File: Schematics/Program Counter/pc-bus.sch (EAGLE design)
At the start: 22 parts

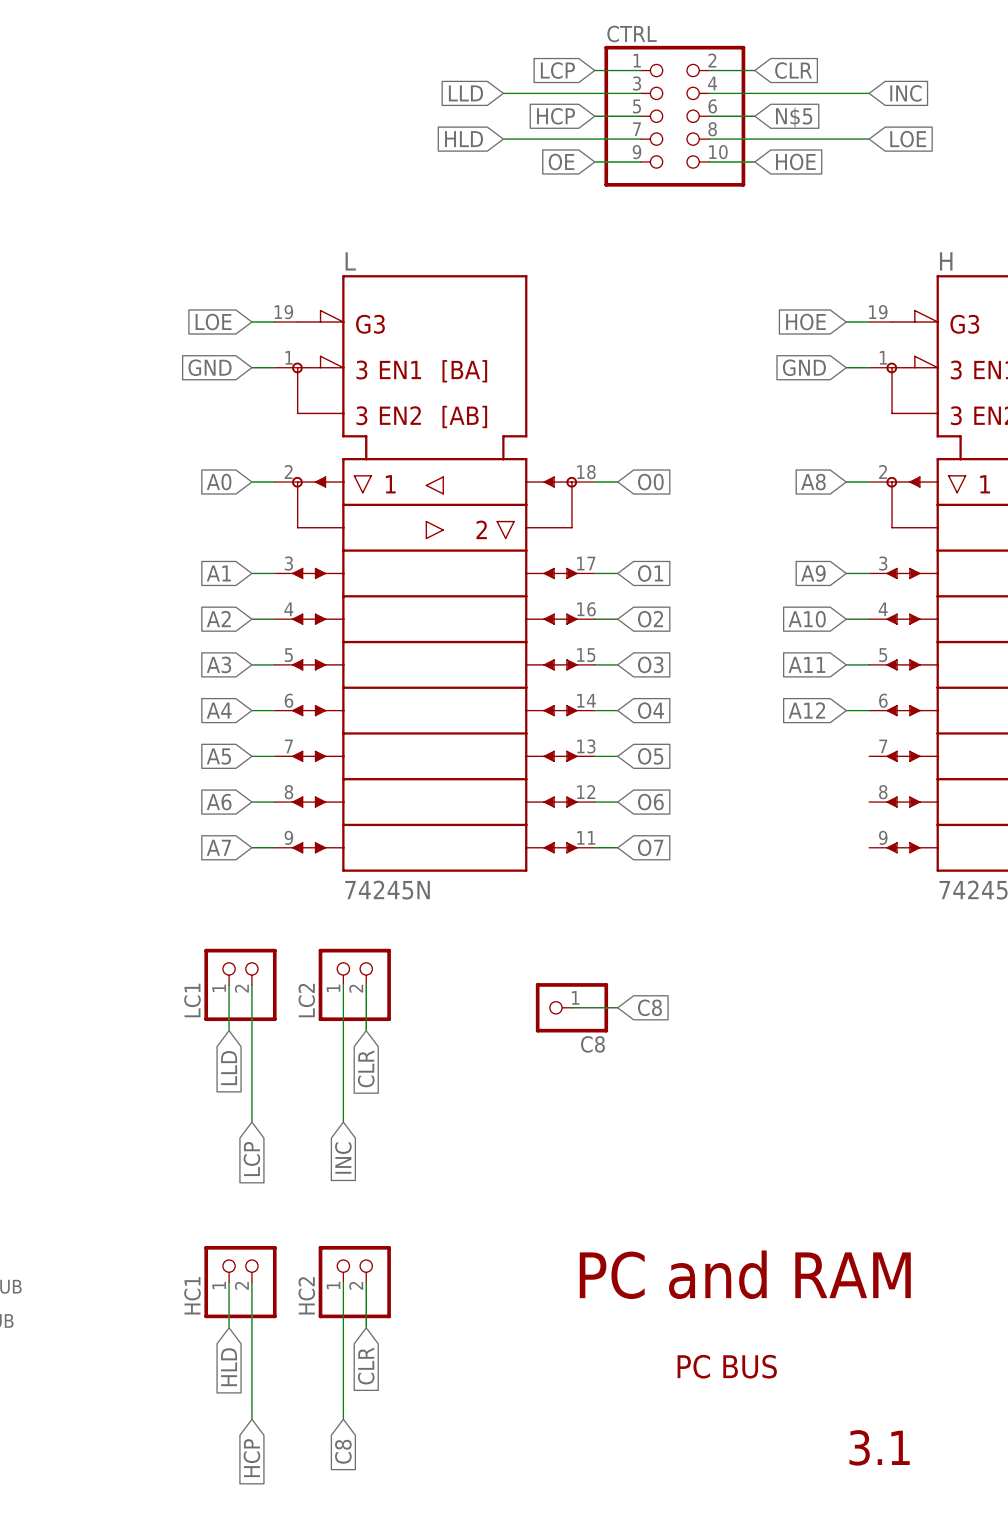
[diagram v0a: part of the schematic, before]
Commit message: Fixed DIR pin on HOE and LOE. Found when I was testing real brd.
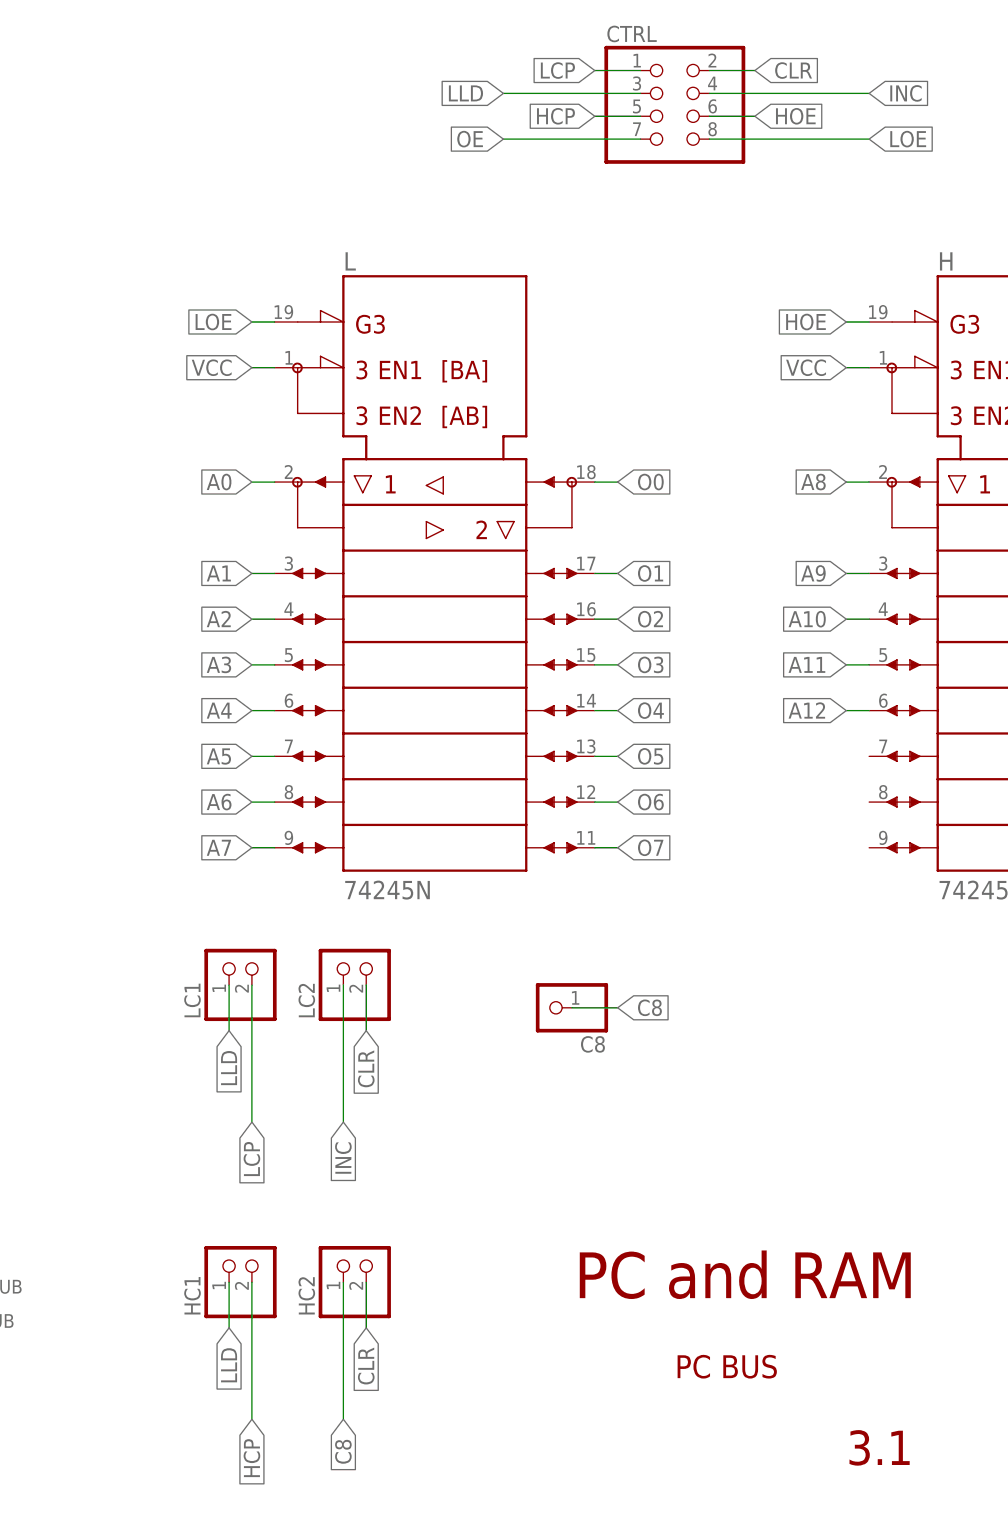
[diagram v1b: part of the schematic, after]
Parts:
- CTRL: device pinhead:PINHD-2X5 -> pinhead:PINHD-2X4
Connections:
- removed net HLD: CTRL.7, HC1.1
- removed net N$5: CTRL.6
- net GND: no longer H1.DIR, L1.DIR
- net HOE: now also CTRL.6; no longer CTRL.10
- net LLD: now also HC1.1
- net OE: now also CTRL.7; no longer CTRL.9
- net VCC: now also H1.DIR, L1.DIR
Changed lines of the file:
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@@
 <part name="H" library="74ttl-din" library_urn="urn:adsk.eagle:library:84" deviceset="74*245" device="N" package3d_urn="urn:adsk.eagle:package:16429/2"/>
 <part name="L" library="74ttl-din" library_urn="urn:adsk.eagle:library:84" deviceset="74*245" device="N" package3d_urn="urn:adsk.eagle:package:16429/2"/>
-<part name="CTRL" library="pinhead" library_urn="urn:adsk.eagle:library:325" deviceset="PINHD-2X5" device="" package3d_urn="urn:adsk.eagle:package:22470/2"/>
 <part name="C8" library="pinhead" library_urn="urn:adsk.eagle:library:325" deviceset="PINHD-1X1" device="" package3d_urn="urn:adsk.eagle:package:22485/2"/>
+<part name="CTRL" library="pinhead" library_urn="urn:adsk.eagle:library:325" deviceset="PINHD-2X4" device="" package3d_urn="urn:adsk.eagle:package:22461/2"/>
 </parts>
 <sheets>
@@
 <attribute name="NAME" x="97.79" y="22.86" size="1.524" layer="95"/>
 </instance>
-<instance part="CTRL" gate="A" x="175.26" y="157.48" smashed="yes">
-<attribute name="NAME" x="168.91" y="165.735" size="1.778" layer="95"/>
-<attribute name="VALUE" x="168.91" y="147.32" size="1.778" layer="96"/>
-</instance>
 <instance part="C8" gate="G$1" x="162.56" y="58.42" smashed="yes" rot="R180">
 <attribute name="NAME" x="168.91" y="55.245" size="1.778" layer="95" rot="R180"/>
 <attribute name="VALUE" x="168.91" y="63.5" size="1.778" layer="96" rot="R180"/>
+</instance>
+<instance part="CTRL" gate="A" x="175.26" y="157.48" smashed="yes">
+<attribute name="NAME" x="168.91" y="165.735" size="1.778" layer="95"/>
+<attribute name="VALUE" x="168.91" y="149.86" size="1.778" layer="96"/>
 </instance>
 </instances>
@@
 <wire x1="71.12" y1="55.88" x2="68.58" y2="55.88" width="0.1524" layer="91"/>
 <label x="71.12" y="55.88" size="1.778" layer="95" xref="yes"/>
+</segment>
+<segment>
+<pinref part="L" gate="1" pin="DIR"/>
+<wire x1="132.08" y1="129.54" x2="129.54" y2="129.54" width="0.1524" layer="91"/>
+<label x="129.54" y="129.54" size="1.778" layer="95" rot="R180" xref="yes"/>
+</segment>
+<segment>
+<pinref part="H" gate="1" pin="DIR"/>
+<wire x1="195.58" y1="129.54" x2="198.12" y2="129.54" width="0.1524" layer="91"/>
+<label x="195.58" y="129.54" size="1.778" layer="95" rot="R180" xref="yes"/>
 </segment>
 </net>
@@
 <label x="71.12" y="45.72" size="1.778" layer="95" xref="yes"/>
 </segment>
-<segment>
-<pinref part="L" gate="1" pin="DIR"/>
-<wire x1="132.08" y1="129.54" x2="129.54" y2="129.54" width="0.1524" layer="91"/>
-<label x="129.54" y="129.54" size="1.778" layer="95" rot="R180" xref="yes"/>
-</segment>
-<segment>
-<pinref part="H" gate="1" pin="DIR"/>
-<wire x1="195.58" y1="129.54" x2="198.12" y2="129.54" width="0.1524" layer="91"/>
-<label x="195.58" y="129.54" size="1.778" layer="95" rot="R180" xref="yes"/>
-</segment>
 </net>
 <net name="B0" class="0">
@@
 </segment>
 <segment>
-<pinref part="CTRL" gate="A" pin="3"/>
 <wire x1="157.48" y1="160.02" x2="172.72" y2="160.02" width="0.1524" layer="91"/>
 <label x="157.48" y="160.02" size="1.778" layer="95" rot="R180" xref="yes"/>
+<pinref part="CTRL" gate="A" pin="3"/>
+</segment>
+<segment>
+<pinref part="HC1" gate="G$1" pin="1"/>
+<wire x1="127" y1="22.86" x2="127" y2="27.94" width="0.1524" layer="91"/>
+<label x="127" y="22.86" size="1.778" layer="95" rot="R270" xref="yes"/>
 </segment>
 </net>
@@
 </segment>
 <segment>
-<pinref part="CTRL" gate="A" pin="1"/>
 <wire x1="167.64" y1="162.56" x2="172.72" y2="162.56" width="0.1524" layer="91"/>
 <label x="167.64" y="162.56" size="1.778" layer="95" rot="R180" xref="yes"/>
+<pinref part="CTRL" gate="A" pin="1"/>
 </segment>
 </net>
@@
 </segment>
 <segment>
-<pinref part="CTRL" gate="A" pin="4"/>
 <wire x1="198.12" y1="160.02" x2="180.34" y2="160.02" width="0.1524" layer="91"/>
 <label x="198.12" y="160.02" size="1.778" layer="95" xref="yes"/>
+<pinref part="CTRL" gate="A" pin="4"/>
 </segment>
 </net>
@@
 </segment>
 <segment>
-<pinref part="CTRL" gate="A" pin="2"/>
 <wire x1="185.42" y1="162.56" x2="180.34" y2="162.56" width="0.1524" layer="91"/>
 <label x="185.42" y="162.56" size="1.778" layer="95" xref="yes"/>
-</segment>
-</net>
-<net name="HLD" class="0">
-<segment>
-<pinref part="HC1" gate="G$1" pin="1"/>
-<wire x1="127" y1="22.86" x2="127" y2="27.94" width="0.1524" layer="91"/>
-<label x="127" y="22.86" size="1.778" layer="95" rot="R270" xref="yes"/>
-</segment>
-<segment>
-<pinref part="CTRL" gate="A" pin="7"/>
-<wire x1="157.48" y1="154.94" x2="172.72" y2="154.94" width="0.1524" layer="91"/>
-<label x="157.48" y="154.94" size="1.778" layer="95" rot="R180" xref="yes"/>
+<pinref part="CTRL" gate="A" pin="2"/>
 </segment>
 </net>
@@
 </segment>
 <segment>
-<pinref part="CTRL" gate="A" pin="5"/>
 <wire x1="167.64" y1="157.48" x2="172.72" y2="157.48" width="0.1524" layer="91"/>
 <label x="167.64" y="157.48" size="1.778" layer="95" rot="R180" xref="yes"/>
+<pinref part="CTRL" gate="A" pin="5"/>
 </segment>
 </net>
@@
 </segment>
 <segment>
-<pinref part="CTRL" gate="A" pin="9"/>
-<wire x1="167.64" y1="152.4" x2="172.72" y2="152.4" width="0.1524" layer="91"/>
-<label x="167.64" y="152.4" size="1.778" layer="95" rot="R180" xref="yes"/>
+<wire x1="157.48" y1="154.94" x2="172.72" y2="154.94" width="0.1524" layer="91"/>
+<label x="157.48" y="154.94" size="1.778" layer="95" rot="R180" xref="yes"/>
+<pinref part="CTRL" gate="A" pin="7"/>
 </segment>
 </net>
@@
 </segment>
 <segment>
-<pinref part="CTRL" gate="A" pin="8"/>
 <wire x1="198.12" y1="154.94" x2="180.34" y2="154.94" width="0.1524" layer="91"/>
 <label x="198.12" y="154.94" size="1.778" layer="95" xref="yes"/>
+<pinref part="CTRL" gate="A" pin="8"/>
 </segment>
 </net>
@@
 </segment>
 <segment>
-<pinref part="CTRL" gate="A" pin="10"/>
-<wire x1="185.42" y1="152.4" x2="180.34" y2="152.4" width="0.1524" layer="91"/>
-<label x="185.42" y="152.4" size="1.778" layer="95" xref="yes"/>
-</segment>
-</net>
-<net name="N$5" class="0">
-<segment>
-<pinref part="CTRL" gate="A" pin="6"/>
 <wire x1="185.42" y1="157.48" x2="180.34" y2="157.48" width="0.1524" layer="91"/>
 <label x="185.42" y="157.48" size="1.778" layer="95" xref="yes"/>
-</segment>
-</net>
+<pinref part="CTRL" gate="A" pin="6"/>
+</segment>
+</net>
